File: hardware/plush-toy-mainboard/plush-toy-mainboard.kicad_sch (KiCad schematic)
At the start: 115 parts, among them U1 ESP32-S3-WROOM-1-N16R8

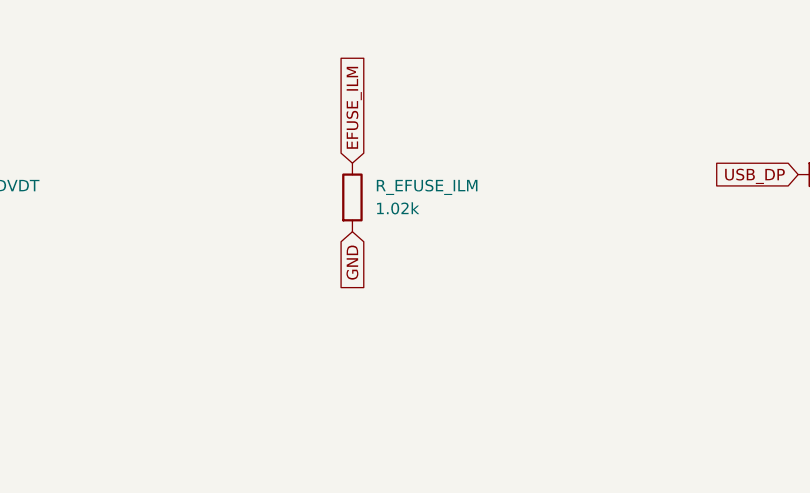
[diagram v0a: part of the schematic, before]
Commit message: fix(pcb): eFuse 限流电阻改 1kΩ，并让 PCB 同步 board_spec 的值
下单时 C226838（1.02kΩ 0402）库存为 0。嘉立创给的三个替代料里，封装对的那颗
可用库存 15 颗но最小贴装量 20 颗，另外两颗是 0201 封装——0201 整颗长 0.6mm，
而 0402 焊盘间隙就有 0.5mm，贴上去两端够不着焊盘，不是勉强能用而是装不上。

改用 1kΩ（C11702，基础库免换料费，库存千万级）：TPS259531 的限流点由 1.9A
变 1.94A，差 2%，离逻辑域 1.5A 峰值仍有余量，且更早动作的是 F_USB 自恢复
保险丝（1.5A 保持电流）。封装仍是 0402，布线与 Gerber 一律不动。

顺带把 1.02k 从 LCSC_R 料号表里删掉，免得以后又选到这颗缺货件。

同时修掉 sync_footprint_metadata 的一个缺口：它只同步料号和装配标志，不同步
值。board_spec 改了阻容值而 PCB 还留着旧值时，DRC 的原理图一致性检查会报差异
（本次实测报 1 条），制造文件也会带着旧值出去。现在值不一致就一并同步。

验证：DRC/未连接/原理图一致性回到只剩 2 条既有的 U1 丝印告警；115 项测试全过；
BOM 与制造文件已重出，全仓已无 1.02k / C226838 残留。

Co-Authored-By: Claude Opus 5 <noreply@anthropic.com>
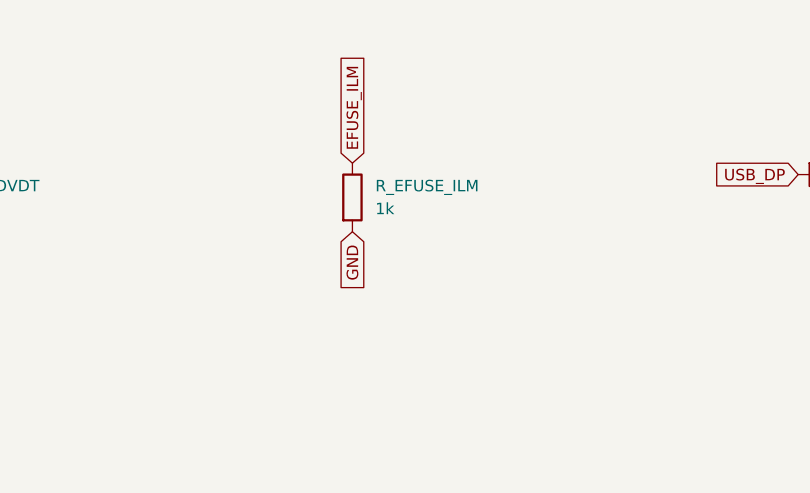
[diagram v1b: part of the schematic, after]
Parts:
- R_EFUSE_ILM: value 1.02k -> 1k; LCSC C226838 -> C11702
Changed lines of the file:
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@@
 			)
 		)
-		(property "Value" "1.02k"
+		(property "Value" "1k"
 			(at 960.12 46.99 0)
 			(effects
@@
 			)
 		)
-		(property "LCSC" "C226838"
+		(property "LCSC" "C11702"
 			(at 957.58 45.72 0)
 			(effects
